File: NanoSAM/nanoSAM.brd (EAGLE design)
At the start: 92 x 89 mm, 76 parts, among them IC3 AD5241, J1 POWER_JACK, U1 LTC3260EMSEPBF

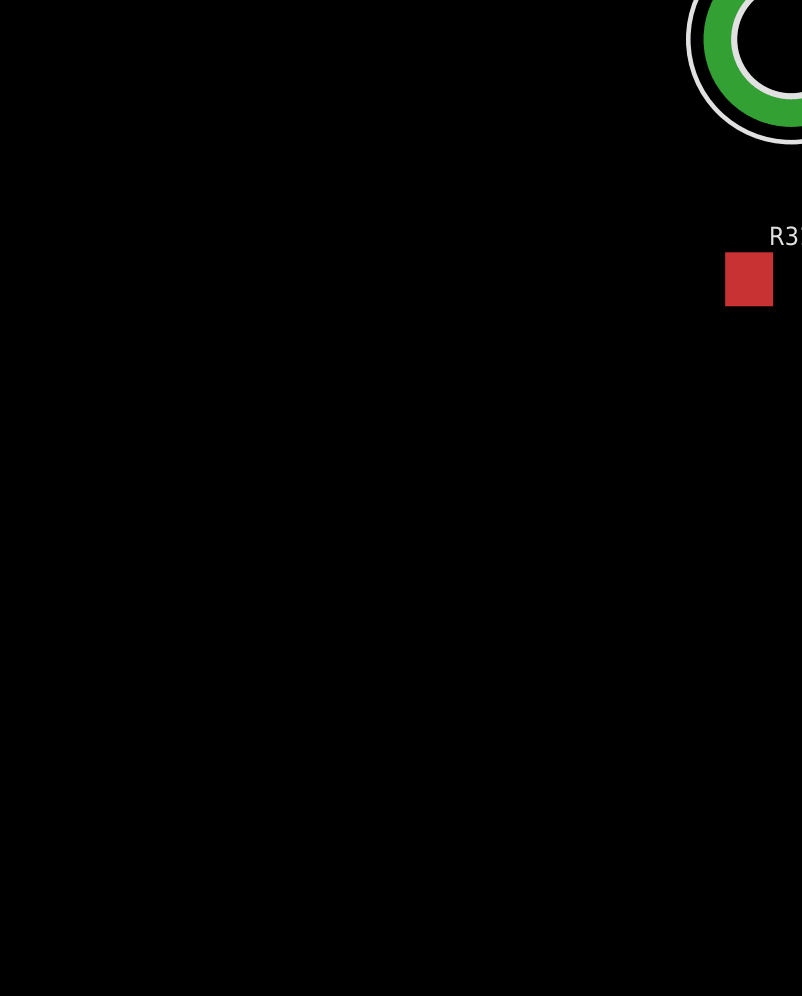
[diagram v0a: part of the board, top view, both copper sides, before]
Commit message: added thermistors for temp monitoring and changed current monitoring circuit
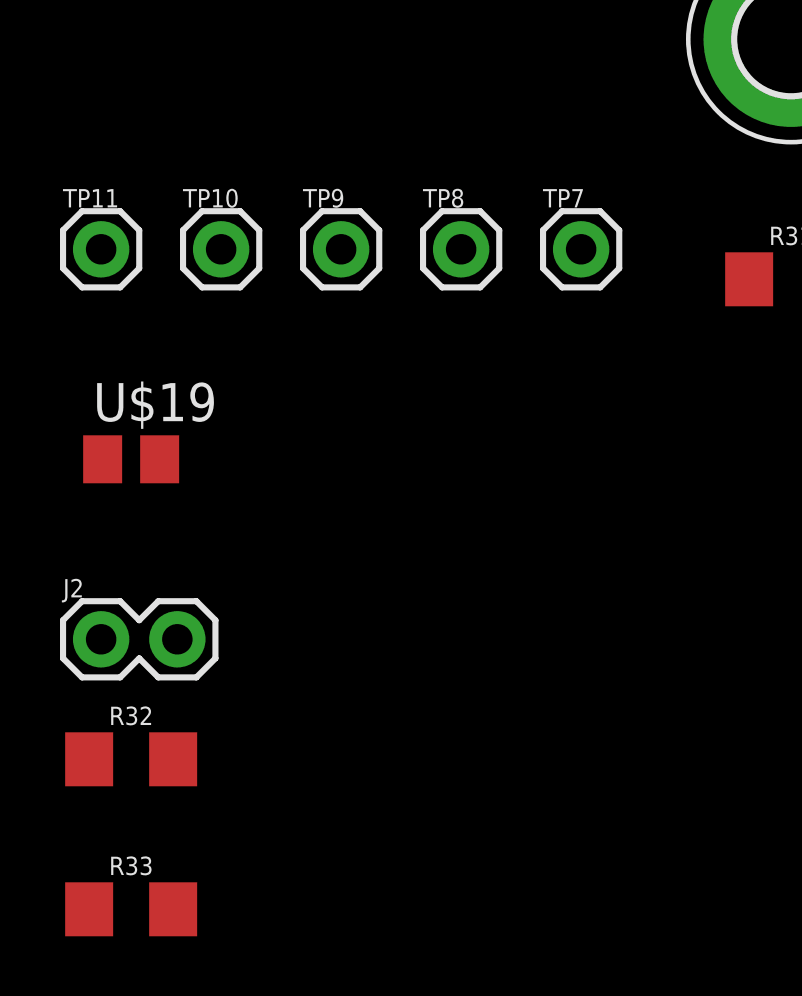
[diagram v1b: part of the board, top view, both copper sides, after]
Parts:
- added J2: (no value), SparkFun-Connectors:1X02
- added R32, R33: 10k, SparkFun-Resistors:1206
- added TP10, TP11, TP7, TP8, TP9: (no value), testpoint:1X01
- added U$19: THERMISTOR, 0805_Thermistor:M0805
- R11, R6: value 1 .1% -> 0.1 .1%
- R12, R13, R17, R18: value 1.00k -> 100
- R16: value 10.0k -> 3.3K
- R19: value 10.0k -> 3.3k
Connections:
- new net HK_BRD_THRM: R32.1, U$19.2
- new net HK_INST_THRM: J2.2, R33.1
- net +3V3: now also R32.2, R33.2
- net AGND: now also TP9.1
- net DGND: now also J2.1, TP10.1, U$19.1
- net N$1: now also TP8.1
- net N$3: now also TP7.1
- net VBUS: now also TP11.1

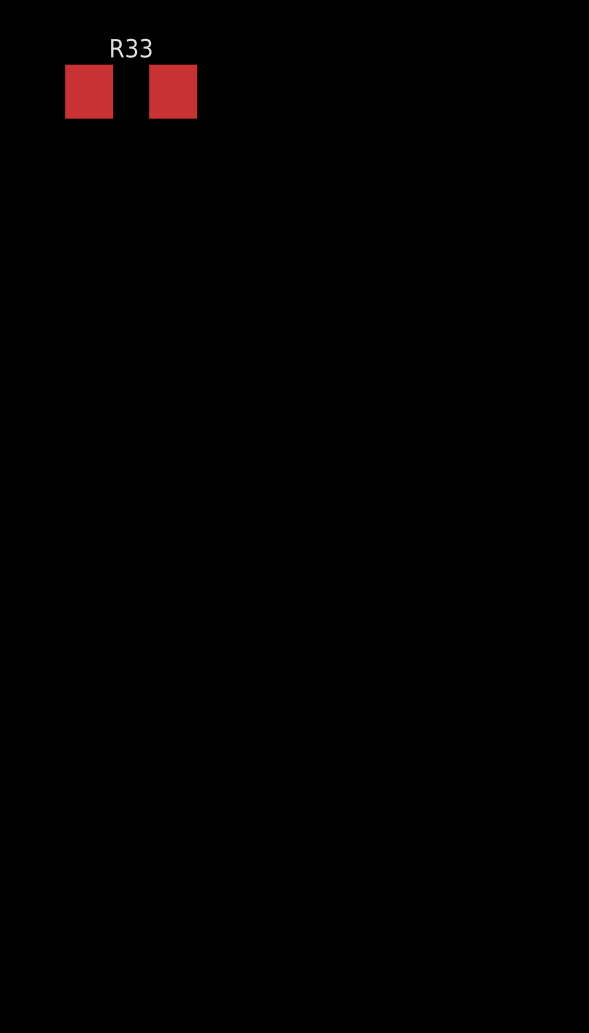
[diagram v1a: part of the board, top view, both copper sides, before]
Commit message: added more thermistor connections
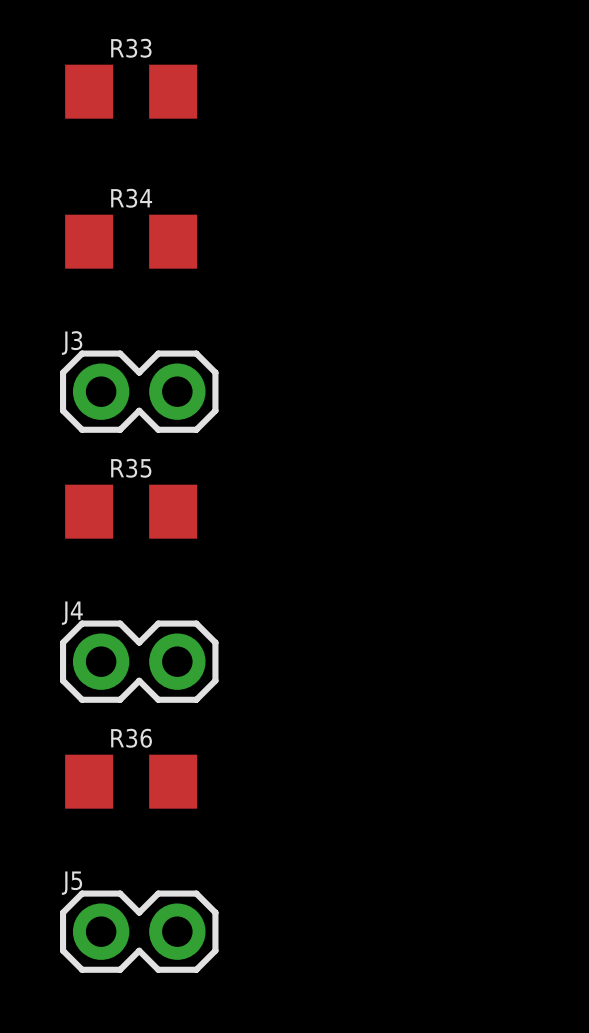
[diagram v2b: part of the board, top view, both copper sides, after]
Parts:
- added J3, J4, J5: (no value), SparkFun-Connectors:1X02
- added R34, R35, R36: 10k, SparkFun-Resistors:1206
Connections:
- removed net HK_INST_THRM: J2.2, R33.1
- removed net HK_THRM: U$2.D17/A3
- removed net N$25: C4.2, IC3.11, IC3.13
- new net HK_INST_THRM0: J2.2, R33.1, U$2.D20/A6
- new net HK_INST_THRM1: J3.2, R34.1, U$2.D21/A7
- new net HK_INST_THRM2: J4.2, R35.1, U$2.D22/A8
- new net HK_INST_THRM3: J5.2, R36.1, U$2.D23/A9
- net +3V3: now also R34.2, R35.2, R36.2
- net DGND: now also C4.2, IC3.11, IC3.13, J3.1, J4.1, J5.1
- net HK_BRD_THRM: now also U$2.D17/A3
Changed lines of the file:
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@@
 <attribute name="VALUE" x="-116" y="-95.143" size="0.6096" layer="27" font="vector" ratio="20" align="top-center"/>
+</element>
+<element name="J3" library="SparkFun-Connectors" library_urn="urn:adsk.eagle:library:513" package="1X02" package3d_urn="urn:adsk.eagle:package:38039/1" value="" x="-117" y="-104" smashed="yes">
+<attribute name="NAME" x="-118.27" y="-102.603" size="0.6096" layer="25" font="vector" ratio="20"/>
+<attribute name="VALUE" x="-118.27" y="-106.032" size="0.6096" layer="27" font="vector" ratio="20"/>
+</element>
+<element name="R34" library="SparkFun-Resistors" library_urn="urn:adsk.eagle:library:532" package="1206" package3d_urn="urn:adsk.eagle:package:39654/1" value="10k" x="-116" y="-99" smashed="yes">
+<attribute name="NAME" x="-116" y="-97.857" size="0.6096" layer="25" font="vector" ratio="20" align="bottom-center"/>
+<attribute name="PROD_ID" value=" " x="-116" y="-103" size="1.778" layer="27" display="off"/>
+<attribute name="VALUE" x="-116" y="-100.143" size="0.6096" layer="27" font="vector" ratio="20" align="top-center"/>
+</element>
+<element name="J4" library="SparkFun-Connectors" library_urn="urn:adsk.eagle:library:513" package="1X02" package3d_urn="urn:adsk.eagle:package:38039/1" value="" x="-117" y="-113" smashed="yes">
+<attribute name="NAME" x="-118.27" y="-111.603" size="0.6096" layer="25" font="vector" ratio="20"/>
+<attribute name="VALUE" x="-118.27" y="-115.032" size="0.6096" layer="27" font="vector" ratio="20"/>
+</element>
+<element name="R35" library="SparkFun-Resistors" library_urn="urn:adsk.eagle:library:532" package="1206" package3d_urn="urn:adsk.eagle:package:39654/1" value="10k" x="-116" y="-108" smashed="yes">
+<attribute name="NAME" x="-116" y="-106.857" size="0.6096" layer="25" font="vector" ratio="20" align="bottom-center"/>
+<attribute name="PROD_ID" value=" " x="-116" y="-112" size="1.778" layer="27" display="off"/>
+<attribute name="VALUE" x="-116" y="-109.143" size="0.6096" layer="27" font="vector" ratio="20" align="top-center"/>
+</element>
+<element name="J5" library="SparkFun-Connectors" library_urn="urn:adsk.eagle:library:513" package="1X02" package3d_urn="urn:adsk.eagle:package:38039/1" value="" x="-117" y="-122" smashed="yes">
+<attribute name="NAME" x="-118.27" y="-120.603" size="0.6096" layer="25" font="vector" ratio="20"/>
+<attribute name="VALUE" x="-118.27" y="-124.032" size="0.6096" layer="27" font="vector" ratio="20"/>
+</element>
+<element name="R36" library="SparkFun-Resistors" library_urn="urn:adsk.eagle:library:532" package="1206" package3d_urn="urn:adsk.eagle:package:39654/1" value="10k" x="-116" y="-117" smashed="yes">
+<attribute name="NAME" x="-116" y="-115.857" size="0.6096" layer="25" font="vector" ratio="20" align="bottom-center"/>
+<attribute name="PROD_ID" value=" " x="-116" y="-121" size="1.778" layer="27" display="off"/>
+<attribute name="VALUE" x="-116" y="-118.143" size="0.6096" layer="27" font="vector" ratio="20" align="top-center"/>
 </element>
 </elements>
@@
 <contactref element="R5" pad="2"/>
 <wire x1="-29.21" y1="38.04" x2="-66.41" y2="54.61" width="0" layer="19" extent="1-1"/>
-</signal>
-<signal name="N$25">
-<contactref element="C4" pad="2"/>
-<contactref element="IC3" pad="13"/>
-<contactref element="IC3" pad="11"/>
-<wire x1="-30.48" y1="43.24" x2="-29.63" y2="59.69" width="0" layer="19" extent="1-1"/>
-<wire x1="-33.02" y1="43.24" x2="-30.48" y2="43.24" width="0" layer="19" extent="1-1"/>
 </signal>
 <signal name="5V">
@@
 <contactref element="U$19" pad="1"/>
 <contactref element="J2" pad="1"/>
+<contactref element="C4" pad="2"/>
+<contactref element="IC3" pad="13"/>
+<contactref element="IC3" pad="11"/>
+<contactref element="J3" pad="1"/>
+<contactref element="J4" pad="1"/>
+<contactref element="J5" pad="1"/>
+<wire x1="-117" y1="-113" x2="-117" y2="-122" width="0" layer="19" extent="1-1"/>
+<wire x1="-117" y1="-104" x2="-117" y2="-113" width="0" layer="19" extent="1-1"/>
+<wire x1="-117" y1="-85" x2="-117" y2="-104" width="0" layer="19" extent="1-1"/>
 <wire x1="-116.95" y1="-79" x2="-117" y2="-85" width="0" layer="19" extent="1-1"/>
 <wire x1="-113" y1="-72" x2="-116.95" y2="-79" width="0" layer="19" extent="1-1"/>
@@
 <wire x1="-46.99" y1="24.13" x2="-48.768" y2="22.098" width="0" layer="19" extent="1-1"/>
 <wire x1="-45.268" y1="22.098" x2="-46.99" y2="24.13" width="0" layer="19" extent="1-1"/>
-<wire x1="-20.32" y1="28.02" x2="-45.268" y2="22.098" width="0" layer="19" extent="1-1"/>
-<wire x1="-15.62" y1="31.02" x2="-20.32" y2="28.02" width="0" layer="19" extent="1-1"/>
-<wire x1="-26.67" y1="43.24" x2="-15.62" y2="31.02" width="0" layer="19" extent="1-1"/>
-<wire x1="-27.94" y1="43.24" x2="-26.67" y2="43.24" width="0" layer="19" extent="1-1"/>
-<wire x1="-29.21" y1="43.24" x2="-27.94" y2="43.24" width="0" layer="19" extent="1-1"/>
+<wire x1="-33.02" y1="43.24" x2="-46.99" y2="24.13" width="0" layer="19" extent="1-1"/>
+<wire x1="-30.48" y1="43.24" x2="-33.02" y2="43.24" width="0" layer="19" extent="1-1"/>
+<wire x1="-29.21" y1="43.24" x2="-30.48" y2="43.24" width="0" layer="19" extent="1-1"/>
+<wire x1="-27.94" y1="43.24" x2="-29.21" y2="43.24" width="0" layer="19" extent="1-1"/>
+<wire x1="-26.67" y1="43.24" x2="-27.94" y2="43.24" width="0" layer="19" extent="1-1"/>
 <wire x1="-27.455" y1="48.26" x2="-27.94" y2="43.24" width="0" layer="19" extent="1-1"/>
 <wire x1="-23.805" y1="47.48" x2="-27.455" y2="48.26" width="0" layer="19" extent="1-1"/>
@@
 <wire x1="-23.805" y1="51.58" x2="-23.805" y2="47.48" width="0" layer="19" extent="1-1"/>
 <wire x1="-24.455" y1="51.58" x2="-23.805" y2="51.58" width="0" layer="19" extent="1-1"/>
-<wire x1="-33.805" y1="48.26" x2="-27.455" y2="48.26" width="0" layer="19" extent="1-1"/>
+<wire x1="-33.805" y1="48.26" x2="-33.02" y2="43.24" width="0" layer="19" extent="1-1"/>
 <wire x1="-25.82" y1="59.69" x2="-24.455" y2="51.58" width="0" layer="19" extent="1-1"/>
-<wire x1="-35.14" y1="59.69" x2="-25.82" y2="59.69" width="0" layer="19" extent="1-1"/>
+<wire x1="-29.63" y1="59.69" x2="-25.82" y2="59.69" width="0" layer="19" extent="1-1"/>
+<wire x1="-35.14" y1="59.69" x2="-29.63" y2="59.69" width="0" layer="19" extent="1-1"/>
 <wire x1="-35.14" y1="63.5" x2="-35.14" y2="59.69" width="0" layer="19" extent="1-1"/>
 <wire x1="-38.95" y1="63.5" x2="-35.14" y2="63.5" width="0" layer="19" extent="1-1"/>
@@
 <wire x1="-63.92" y1="63.5" x2="-56.3" y2="63.5" width="0" layer="19" extent="1-1"/>
 <wire x1="-13.84" y1="54.61" x2="-23.805" y2="51.58" width="0" layer="19" extent="1-1"/>
+<wire x1="-15.62" y1="31.02" x2="-26.67" y2="43.24" width="0" layer="19" extent="1-1"/>
+<wire x1="-20.32" y1="28.02" x2="-15.62" y2="31.02" width="0" layer="19" extent="1-1"/>
 <wire x1="-87.63" y1="35.56" x2="-57.15" y2="27.01" width="0" layer="19" extent="1-1"/>
 </signal>
@@
 <contactref element="R32" pad="2"/>
 <contactref element="R33" pad="2"/>
+<contactref element="R34" pad="2"/>
+<contactref element="R35" pad="2"/>
+<contactref element="R36" pad="2"/>
+<wire x1="-114.6" y1="-108" x2="-114.6" y2="-117" width="0" layer="19" extent="1-1"/>
+<wire x1="-114.6" y1="-99" x2="-114.6" y2="-108" width="0" layer="19" extent="1-1"/>
+<wire x1="-114.6" y1="-94" x2="-114.6" y2="-99" width="0" layer="19" extent="1-1"/>
 <wire x1="-114.6" y1="-89" x2="-114.6" y2="-94" width="0" layer="19" extent="1-1"/>
 <wire x1="-88.53" y1="-10.16" x2="-114.6" y2="-89" width="0" layer="19" extent="1-1"/>
@@
 <wire x1="-72.39" y1="30.48" x2="-74.93" y2="2.54" width="0" layer="19" extent="1-1"/>
 </signal>
-<signal name="HK_THRM">
-<contactref element="U$2" pad="D17/A3"/>
-</signal>
 <signal name="FLASH_CS1">
 <contactref element="U$16" pad="1"/>
@@
 <contactref element="R32" pad="1"/>
 <contactref element="U$19" pad="2"/>
+<contactref element="U$2" pad="D17/A3"/>
 <wire x1="-115.05" y1="-79" x2="-117.4" y2="-89" width="0" layer="19" extent="1-1"/>
-</signal>
-<signal name="HK_INST_THRM">
+<wire x1="-72.39" y1="12.7" x2="-115.05" y2="-79" width="0" layer="19" extent="1-1"/>
+</signal>
+<signal name="HK_INST_THRM1">
+<contactref element="R34" pad="1"/>
+<contactref element="J3" pad="2"/>
+<contactref element="U$2" pad="D21/A7"/>
+<wire x1="-117.4" y1="-99" x2="-114.46" y2="-104" width="0" layer="19" extent="1-1"/>
+<wire x1="-72.39" y1="22.86" x2="-117.4" y2="-99" width="0" layer="19" extent="1-1"/>
+</signal>
+<signal name="HK_INST_THRM2">
+<contactref element="R35" pad="1"/>
+<contactref element="J4" pad="2"/>
+<contactref element="U$2" pad="D22/A8"/>
+<wire x1="-117.4" y1="-108" x2="-114.46" y2="-113" width="0" layer="19" extent="1-1"/>
+<wire x1="-72.39" y1="25.4" x2="-117.4" y2="-108" width="0" layer="19" extent="1-1"/>
+</signal>
+<signal name="HK_INST_THRM3">
+<contactref element="R36" pad="1"/>
+<contactref element="J5" pad="2"/>
+<contactref element="U$2" pad="D23/A9"/>
+<wire x1="-117.4" y1="-117" x2="-114.46" y2="-122" width="0" layer="19" extent="1-1"/>
+<wire x1="-72.39" y1="27.94" x2="-117.4" y2="-117" width="0" layer="19" extent="1-1"/>
+</signal>
+<signal name="HK_INST_THRM0">
 <contactref element="R33" pad="1"/>
 <contactref element="J2" pad="2"/>
+<contactref element="U$2" pad="D20/A6"/>
 <wire x1="-114.46" y1="-85" x2="-117.4" y2="-94" width="0" layer="19" extent="1-1"/>
+<wire x1="-72.39" y1="20.32" x2="-114.46" y2="-85" width="0" layer="19" extent="1-1"/>
 </signal>
 </signals>

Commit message: started layout
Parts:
- moved J5 271.2 mm to (57.0, 86.0)
- moved J4 269.0 mm to (64.0, 86.0)
- moved J3 267.3 mm to (71.0, 86.0)
- moved J2 259.4 mm to (78.0, 86.0)
- moved H2 227.2 mm to (90.8, 85.1)
- moved U$19 203.2 mm to (45.0, 45.0), turned to 270 degrees
- moved H3 194.6 mm to (90.8, 5.08)
- moved U$17 184.9 mm to (64.4, 70.0), turned to 90 degrees
- moved H4 177.8 mm to (5.08, 82.6)
- moved U$16 171.2 mm to (64.5, 62.0), turned to 90 degrees
- moved U$2 150.9 mm to (68.9, 44.8), turned to 270 degrees
- moved L2 149.7 mm to (85.9, 14.5), turned to 90 degrees
- moved U$12 123.5 mm to (76.1, 14.0), turned to 270 degrees
- moved H1 118.3 mm to (5.08, 8.90)
- moved U$5 105.5 mm to (37.0, 67.9), turned to 90 degrees
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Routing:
- net AGND: track 0.00 -> 1.37 mm, vias 0 -> 1
- added copper zone on layer 2, net AGND
- added copper zone on layer 2, net DGND
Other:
- board size 92 x 89 mm -> 95.9 x 90.2 mm

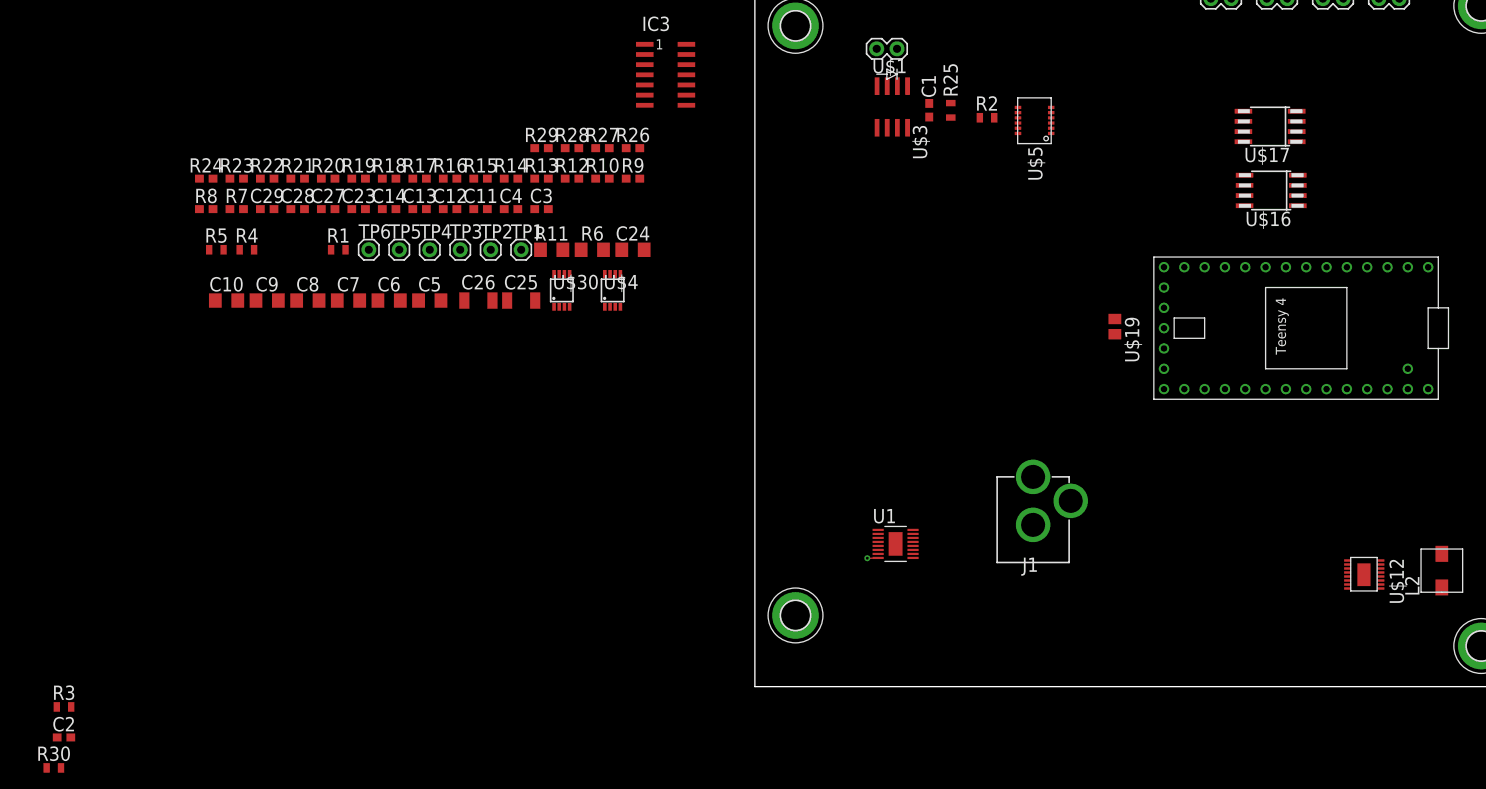
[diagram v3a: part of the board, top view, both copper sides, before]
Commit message: routed analog signals, added R3 and C2 by microcontroller
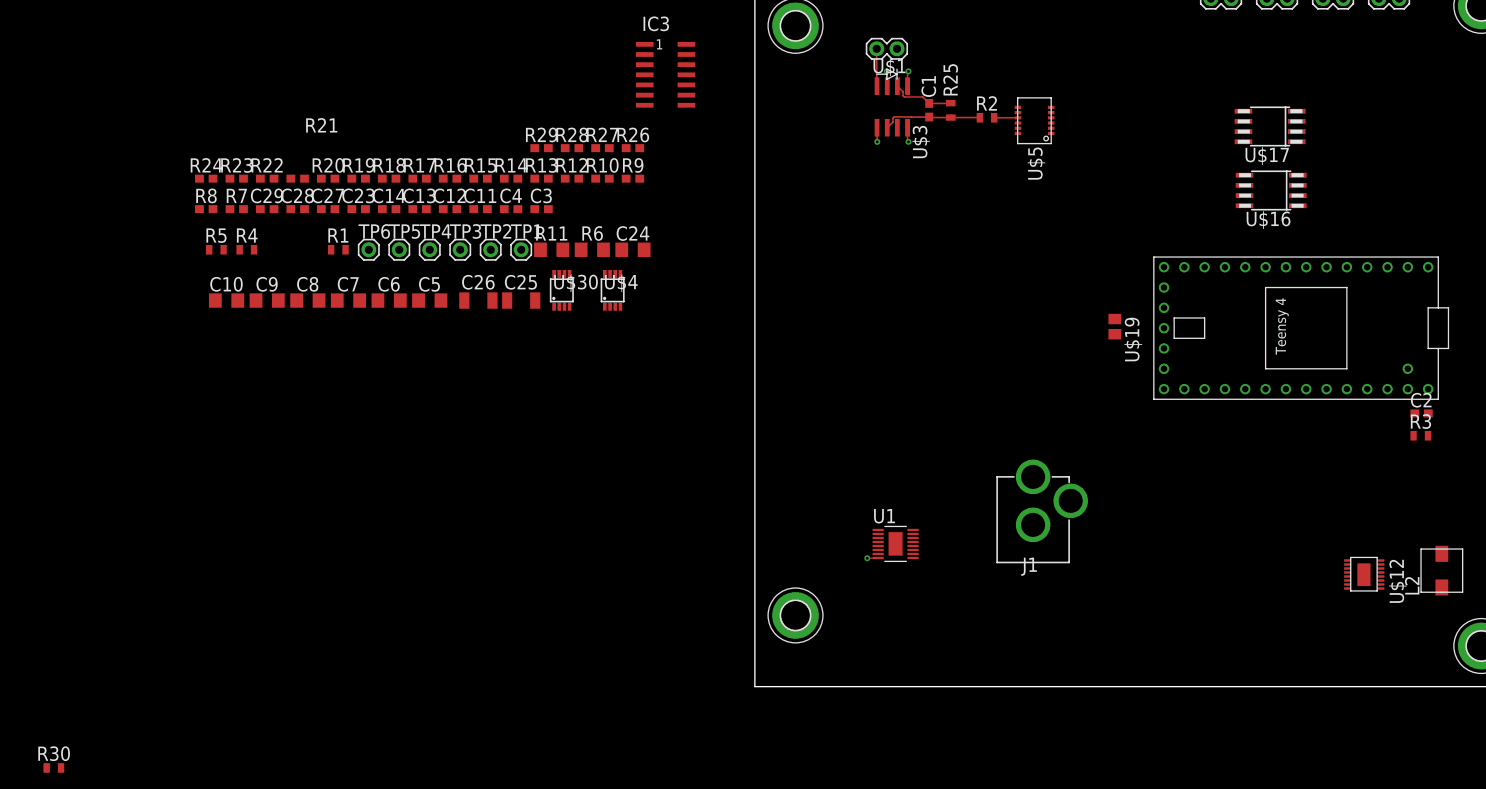
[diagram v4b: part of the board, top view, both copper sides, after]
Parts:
- moved C2 174.5 mm to (83.3, 34.1)
- moved R3 173.0 mm to (83.2, 31.4)
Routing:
- net N$2: track 0.00 -> 12.5 mm
- net N$1: track 0.00 -> 7.87 mm
- net AGND: track 1.37 -> 8.69 mm, vias 1 -> 5
- net VNEG: track 0.00 -> 4.69 mm
- net N$3: track 0.00 -> 2.97 mm
